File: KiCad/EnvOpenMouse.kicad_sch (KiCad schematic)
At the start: 49 parts, among them J1 SKRKAEE020, J2 SKRKAEE020, J3 Conn_01x03_Male, SW1 MouseSwitch, SW2 MouseSwitch, U1 TCR2EF19, U2 LM3671MF 3.3, U3 PMW3360DM-T2QU, U4 RP2040, Y1 Crystal 3225 12MHz

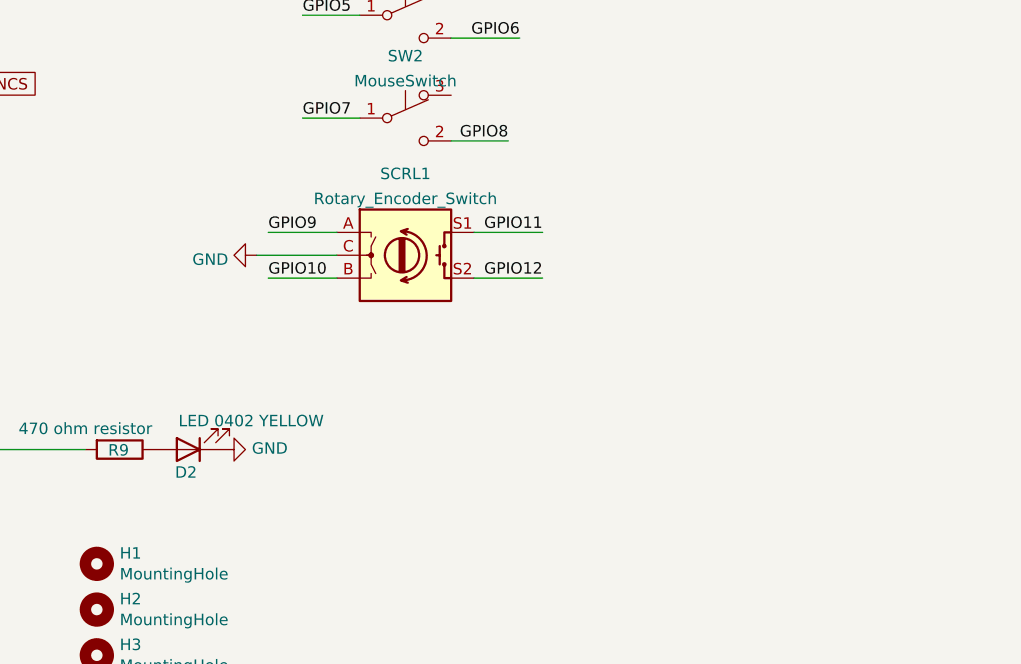
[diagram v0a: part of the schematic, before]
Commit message: added some GPIO headers
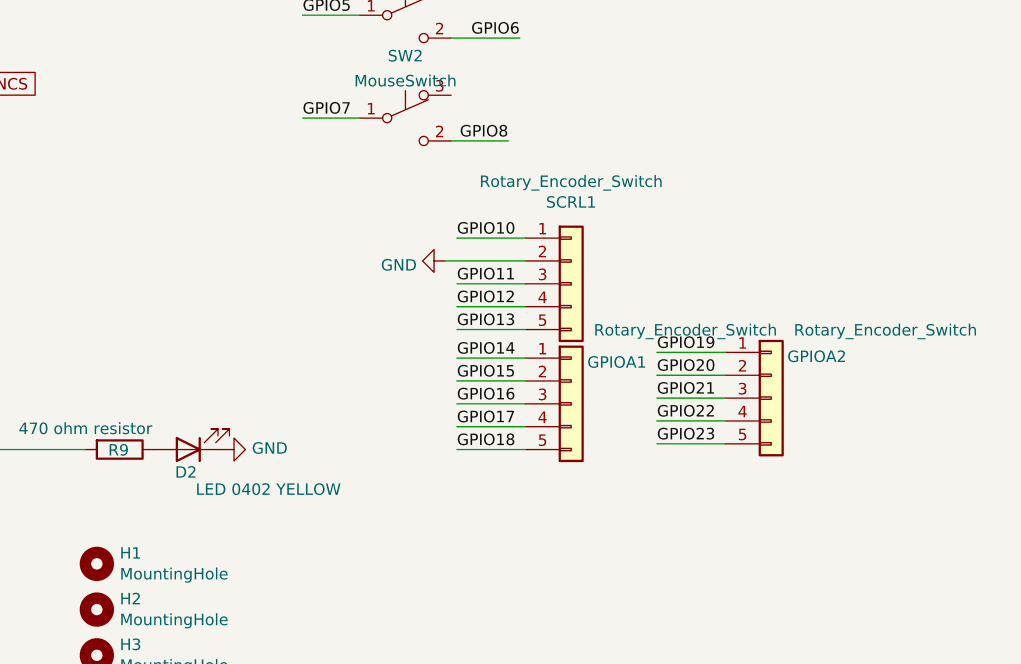
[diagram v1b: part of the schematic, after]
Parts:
- added GPIOA1, GPIOA2: Rotary_Encoder_Switch, Connector_PinHeader_2.54mm:PinHeader_1x05_P2.54mm_Vertical, symbol Connector_Generic:Conn_01x05
- SCRL1: footprint (none) -> Connector_PinHeader_2.54mm:PinHeader_1x05_P2.54mm_Vertical; symbol Device:Rotary_Encoder_Switch -> Connector_Generic:Conn_01x05
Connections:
- net GND: now also SCRL1.2 (Pin_2); no longer SCRL1.C
- net GPIO10: now also SCRL1.1 (Pin_1); no longer SCRL1.B
- net GPIO11: now also SCRL1.3 (Pin_3); no longer SCRL1.S1
- net GPIO12: now also SCRL1.4 (Pin_4); no longer SCRL1.S2
- net GPIO13: now also SCRL1.5 (Pin_5)
- net GPIO14: now also GPIOA1.1 (Pin_1)
- net GPIO15: now also GPIOA1.2 (Pin_2)
- net GPIO16: now also GPIOA1.3 (Pin_3)
- net GPIO17: now also GPIOA1.4 (Pin_4)
- net GPIO18: now also GPIOA1.5 (Pin_5)
- net GPIO19: now also GPIOA2.1 (Pin_1)
- net GPIO20: now also GPIOA2.2 (Pin_2)
- net GPIO21: now also GPIOA2.3 (Pin_3)
- net GPIO22: now also GPIOA2.4 (Pin_4)
- net GPIO23: now also GPIOA2.5 (Pin_5)
- net NCS: no longer SCRL1.A

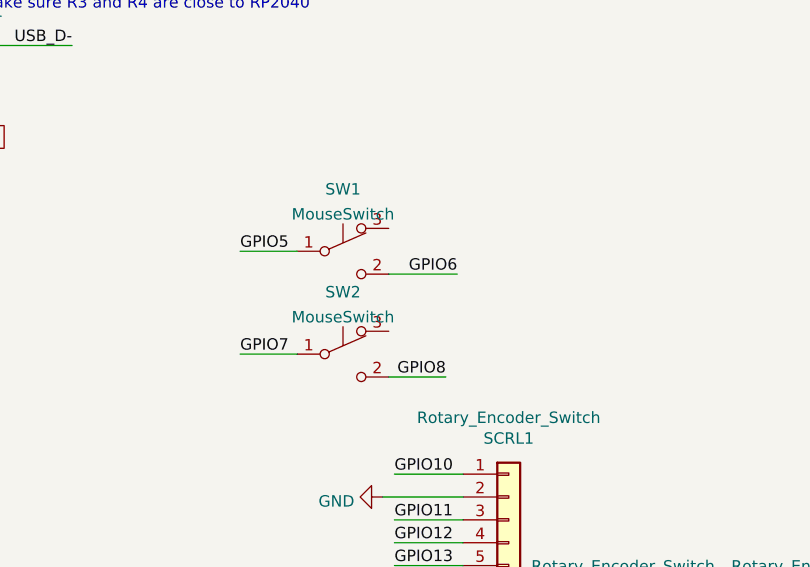
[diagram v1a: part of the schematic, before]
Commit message: swapped button bits for some GPIO headers
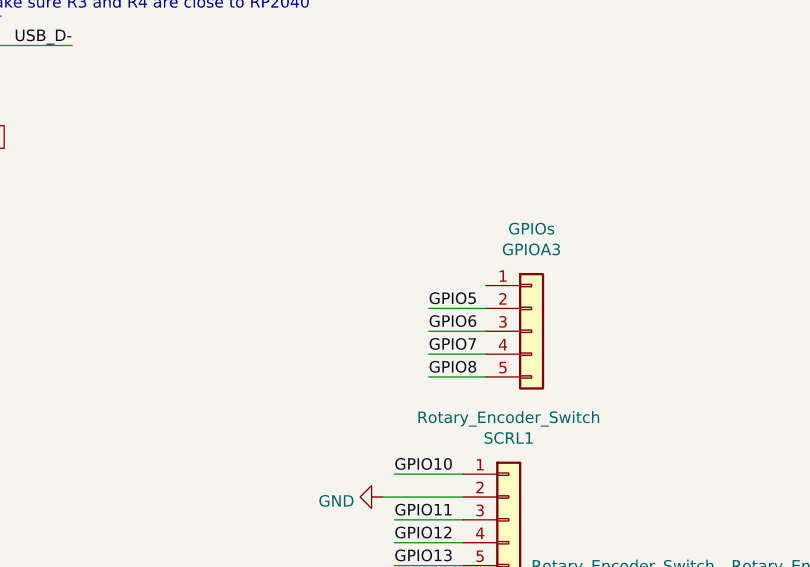
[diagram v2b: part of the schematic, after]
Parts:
- removed SW1, SW2: MouseSwitch, MouseSwitch:MouseSwitch, symbol Switch:SW_Push_SPDT
- added GPIOA3: GPIOs, Connector_PinHeader_2.54mm:PinHeader_1x05_P2.54mm_Vertical, symbol Connector_Generic:Conn_01x05
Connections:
- net GPIO5: now also GPIOA3.2 (Pin_2)
- net GPIO6: now also GPIOA3.3 (Pin_3)
- net GPIO7: now also GPIOA3.4 (Pin_4)
- net GPIO8: now also GPIOA3.5 (Pin_5)
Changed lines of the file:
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@@
-    (stroke (width 0) (type default) (color 0 0 0 0))
-  )
-  (wire (pts (xy 257.81 180.34) (xy 264.16 180.34))
-    (stroke (width 0) (type default) (color 0 0 0 0))
-  )
-  (wire (pts (xy 257.81 191.77) (xy 264.16 191.77))
     (stroke (width 0) (type default) (color 0 0 0 0))
   )
@@
     (stroke (width 0) (type default) (color 0 0 0 0))
   )
-  (wire (pts (xy 274.32 182.88) (xy 281.94 182.88))
-    (stroke (width 0) (type default) (color 0 0 0 0))
-  )
-  (wire (pts (xy 274.32 194.31) (xy 280.67 194.31))
-    (stroke (width 0) (type default) (color 0 0 0 0))
-  )
   (wire (pts (xy 274.701 114.3) (xy 274.701 115.57))
     (stroke (width 0) (type solid) (color 0 0 0 0))
@@
     (stroke (width 0) (type default) (color 0 0 0 0))
   )
+  (wire (pts (xy 278.765 186.69) (xy 285.115 186.69))
+    (stroke (width 0) (type default) (color 0 0 0 0))
+  )
+  (wire (pts (xy 278.765 191.77) (xy 285.115 191.77))
+    (stroke (width 0) (type default) (color 0 0 0 0))
+  )
+  (wire (pts (xy 278.765 194.31) (xy 285.115 194.31))
+    (stroke (width 0) (type default) (color 0 0 0 0))
+  )
   (wire (pts (xy 282.575 210.185) (xy 274.955 210.185))
     (stroke (width 0) (type default) (color 0 0 0 0))
   )
   (wire (pts (xy 282.575 212.725) (xy 274.955 212.725))
+    (stroke (width 0) (type default) (color 0 0 0 0))
+  )
+  (wire (pts (xy 285.115 189.23) (xy 278.765 189.23))
     (stroke (width 0) (type default) (color 0 0 0 0))
   )
@@
     (effects (font (size 1.27 1.27)) (justify right bottom))
   )
-  (label "GPIO5" (at 257.81 180.34 0)
-    (effects (font (size 1.27 1.27)) (justify left bottom))
-  )
-  (label "GPIO7" (at 257.81 191.77 0)
-    (effects (font (size 1.27 1.27)) (justify left bottom))
-  )
   (label "GPIO10" (at 274.955 205.105 0)
     (effects (font (size 1.27 1.27)) (justify left bottom))
@@
     (effects (font (size 1.27 1.27)) (justify left bottom))
   )
-  (label "GPIO8" (at 280.67 194.31 180)
-    (effects (font (size 1.27 1.27)) (justify right bottom))
-  )
-  (label "GPIO6" (at 281.94 182.88 180)
-    (effects (font (size 1.27 1.27)) (justify right bottom))
+  (label "GPIO5" (at 278.765 186.69 0)
+    (effects (font (size 1.27 1.27)) (justify left bottom))
+  )
+  (label "GPIO6" (at 278.765 189.23 0)
+    (effects (font (size 1.27 1.27)) (justify left bottom))
+  )
+  (label "GPIO7" (at 278.765 191.77 0)
+    (effects (font (size 1.27 1.27)) (justify left bottom))
+  )
+  (label "GPIO8" (at 278.765 194.31 0)
+    (effects (font (size 1.27 1.27)) (justify left bottom))
   )
   (label "GPIO19" (at 297.18 217.805 0)
@@
     (pin "3")
   )
-  (symbol (lib_name "SW_Push_SPDT_1") (lib_id "Switch:SW_Push_SPDT") (at 269.24 180.34 0) (unit 1)
-    (in_bom yes) (on_board yes) (fields_autoplaced)
-    (property "Reference" "SW1" (id 0) (at 269.24 173.4525 0))
-    (property "Value" "MouseSwitch" (id 1) (at 269.24 176.2276 0))
-    (property "Footprint" "MouseSwitch:MouseSwitch" (id 2) (at 269.24 180.34 0)
-      (effects (font (size 1.27 1.27)) hide)
-    )
-    (property "Datasheet" "~" (id 3) (at 269.24 180.34 0)
-      (effects (font (size 1.27 1.27)) hide)
-    )
-    (pin "1")
-    (pin "2")
-    (pin "3")
-  )
-  (symbol (lib_name "SW_Push_SPDT_1") (lib_id "Switch:SW_Push_SPDT") (at 269.24 191.77 0) (unit 1)
-    (in_bom yes) (on_board yes) (fields_autoplaced)
-    (property "Reference" "SW2" (id 0) (at 269.24 184.8825 0))
-    (property "Value" "MouseSwitch" (id 1) (at 269.24 187.6576 0))
-    (property "Footprint" "MouseSwitch:MouseSwitch" (id 2) (at 269.24 191.77 0)
-      (effects (font (size 1.27 1.27)) hide)
-    )
-    (property "Datasheet" "~" (id 3) (at 269.24 191.77 0)
-      (effects (font (size 1.27 1.27)) hide)
-    )
-    (pin "1")
-    (pin "2")
-    (pin "3")
-  )
   (symbol (lib_id "logo:LOGO") (at 307.34 264.16 0) (unit 1)
     (in_bom yes) (on_board yes)
@@
     )
     (property "Datasheet" "~" (id 3) (at 287.655 223.52 0)
+      (effects (font (size 1.27 1.27)) hide)
+    )
+    (pin "1")
+    (pin "2")
+    (pin "3")
+    (pin "4")
+    (pin "5")
+  )
+  (symbol (lib_id "Connector_Generic:Conn_01x05") (at 290.195 189.23 0) (unit 1)
+    (in_bom yes) (on_board yes)
+    (property "Reference" "GPIOA3" (id 0) (at 290.195 180.1835 0))
+    (property "Value" "GPIOs" (id 1) (at 290.195 177.8786 0))
+    (property "Footprint" "Connector_PinHeader_2.54mm:PinHeader_1x05_P2.54mm_Vertical" (id 2) (at 290.195 189.23 0)
+      (effects (font (size 1.27 1.27)) hide)
+    )
+    (property "Datasheet" "~" (id 3) (at 290.195 189.23 0)
       (effects (font (size 1.27 1.27)) hide)
     )
@@
       (reference "GPIOA2") (unit 1) (value "Rotary_Encoder_Switch") (footprint "Connector_PinHeader_2.54mm:PinHeader_1x05_P2.54mm_Vertical")
     )
+    (path "/2f2d64a6-47ea-4791-ab5a-ecbf732b2941"
+      (reference "GPIOA3") (unit 1) (value "GPIOs") (footprint "Connector_PinHeader_2.54mm:PinHeader_1x05_P2.54mm_Vertical")
+    )
     (path "/00000000-0000-0000-0000-00005ef4c292"
       (reference "H1") (unit 1) (value "MountingHole") (footprint "MountingHole:MountingHole_2.2mm_M2")
@@
       (reference "SCRL1") (unit 1) (value "Rotary_Encoder_Switch") (footprint "Connector_PinHeader_2.54mm:PinHeader_1x05_P2.54mm_Vertical")
     )
-    (path "/798c83d4-bf59-4ae7-be16-94ab000014d2"
-      (reference "SW1") (unit 1) (value "MouseSwitch") (footprint "MouseSwitch:MouseSwitch")
-    )
-    (path "/9c1369db-a523-40cf-ba52-a05103bcd1ac"
-      (reference "SW2") (unit 1) (value "MouseSwitch") (footprint "MouseSwitch:MouseSwitch")
-    )
     (path "/d68793be-7291-4680-8a60-4689160c349c"

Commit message: decided to overhaul this project a bit
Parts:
- removed C1: 10uf 0603 6.3V, Capacitor_SMD:C_0603_1608Metric, symbol Device:C
- removed C10, C11, C12, C13, C14, C17, C6, C7, C8, C9: 100nf 0402, Capacitor_SMD:C_0402_1005Metric, symbol Device:C
- removed C15, C16: 1uf 0402, Capacitor_SMD:C_0402_1005Metric, symbol Device:C
- removed C18, C19: 22pf 0402, Capacitor_SMD:C_0402_1005Metric, symbol Device:C
- removed C4: 10uf 0402, Capacitor_SMD:C_0402_1005Metric, symbol Device:C
- removed D1: 1n4002 0603, Diode_SMD:D_0603_1608Metric, symbol Device:D_Schottky
- removed D2: LED 0402 YELLOW, LED_SMD:LED_0402_1005Metric, symbol Device:LED
- removed FLASH1: W25Q16FWUXIE, Package_SON:SON-8-1EP_3x2mm_P0.5mm_EP1.4x1.6mm, symbol W25Q256JVEIQ_TR:W25Q256JVEIQ_TR
- removed GPIOA1, GPIOA2, SCRL1: Rotary_Encoder_Switch, Connector_PinHeader_2.54mm:PinHeader_1x05_P2.54mm_Vertical, symbol Connector_Generic:Conn_01x05
- removed GPIOA3: GPIOs, Connector_PinHeader_2.54mm:PinHeader_1x05_P2.54mm_Vertical, symbol Connector_Generic:Conn_01x05
- removed H1, H2, H3, H4: MountingHole, MountingHole:MountingHole_2.2mm_M2, symbol Mechanical:MountingHole
- removed J1, J2: SKRKAEE020, Button_Switch_SMD:SW_Push_SPST_NO_Alps_SKRK, symbol Switch:SW_Push
- removed L1: INDUCTOR 2.2uH 0805, Inductor_SMD:L_0805_2012Metric, symbol pspice:INDUCTOR
- removed R10: 1K 0402, Resistor_SMD:R_0402_1005Metric, symbol Device:R_Small
- removed R2, R4: 5.1K, Resistor_SMD:R_0402_1005Metric, symbol Device:R_Small
- removed R5: 10K 0402, Capacitor_SMD:C_0402_1005Metric, symbol Device:R
- removed R6, R7: 27Ohms 0402 Resistor, Capacitor_SMD:C_0402_1005Metric, symbol Device:R
- removed R8: 1k 0402 Resistor, Capacitor_SMD:C_0402_1005Metric, symbol Device:R
- removed R9: 470 ohm resistor, Resistor_SMD:R_0402_1005Metric, symbol Device:R
- removed U2: LM3671MF 3.3, Package_TO_SOT_SMD:SOT-23-5, symbol Regulator_Switching:LM3670MF
- removed U4: RP2040, env:RP2040-QFN-56, symbol MCU_RaspberryPi_RP2040:RP2040
- removed Y1: Crystal 3225 12MHz, Crystal:Crystal_SMD_3225-4Pin_3.2x2.5mm, symbol Device:Crystal_GND24
- removed e1: TYPE-C-31-M-12, Type-C:HRO-TYPE-C-31-M-12-Assembly, symbol Type-C:HRO-TYPE-C-31-M-12
- added H1, H10, H2, H3, H4, H5, H6, H7, H8, H9: MountingHole_Pad, MountingHole:MountingHole_2.2mm_M2, symbol Mechanical:MountingHole_Pad
- added J1: Conn_01x08, Connector_PinHeader_1.00mm:PinHeader_1x08_P1.00mm_Vertical, symbol Connector_Generic:Conn_01x08
- added J2: Conn_01x03, Connector_PinSocket_2.54mm:PinSocket_1x03_P2.54mm_Vertical, symbol Connector_Generic:Conn_01x03
- added J4: Conn_01x03, Connector_PinHeader_2.54mm:PinHeader_1x03_P2.54mm_Vertical, symbol Connector_Generic:Conn_01x03
- added SW1, SW2: SW_Push_SPDT, MouseSwitch:MouseSwitch, symbol Switch:SW_Push_SPDT
- added VR1: EC10E1220501, EC10E1220501:TRIM_EC10E1220501, symbol EC10E1220501:EC10E1220501
- C1: renamed from C2; footprint Capacitor_SMD:C_0402_1005Metric -> Capacitor_SMD:C_0201_0603Metric
- C2: renamed from C3; footprint Capacitor_SMD:C_0402_1005Metric -> Capacitor_SMD:C_0201_0603Metric
- C3: renamed from C5; footprint Capacitor_SMD:C_0402_1005Metric -> Capacitor_SMD:C_0201_0603Metric
- J3: value Conn_01x03_Male -> Conn_01x03; footprint Connector_PinHeader_2.54mm:PinHeader_1x03_P2.54mm_Vertical -> Connector_PinSocket_2.54mm:PinSocket_1x03_P2.54mm_Vertical
- renumbered R3 to R2, U3 to U2
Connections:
- net +3V3: now also J1.6 (Pin_6)
- net +5V: now also J1.7 (Pin_7)
- net GND: now also H1.1, H10.1, H2.1, H3.1, H4.1, H5.1, H6.1, H7.1, H8.1, H9.1, J1.8 (Pin_8); no longer J3.2 (Pin_2)
- net MISO renamed MISO/GPIO4
- net MISO/GPIO4: now also J1.2 (Pin_2)
- net MOSI renamed MOSI/GPIO3
- net MOSI/GPIO3: now also J1.3 (Pin_3)
- net MOTION renamed MOTION/GPIO1
- net MOTION/GPIO1: now also J1.5 (Pin_5)
- net NCS renamed NCS/GPIO9
- net NCS/GPIO9: now also J1.1 (Pin_1)
- net SCLK renamed SCLK/GPIO2
- net SCLK/GPIO2: now also J1.4 (Pin_4)
- net SWCLK: no longer names the net of J3.1 (Pin_1)
- net SWCLK: now also SW2.1 (A)
- net SWD: no longer names the net of J3.3 (Pin_3)
- net SWD: now also SW2.3 (C)
- new net: J2.1 (Pin_1), SW1.1 (A)
- new net: J2.2 (Pin_2), SW1.2 (B)
- new net: J2.3 (Pin_3), SW1.3 (C)
- new net: J4.1 (Pin_1), VR1.C
- new net: J4.2 (Pin_2), VR1.B
- new net: J4.3 (Pin_3), VR1.A
- new net: J3.2 (Pin_2), SW2.2 (B)
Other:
- note added: "1.8V regulator"
- note added: "Mount Holes"
- note added: "Mouse Buttons"
- note added: "Scroll Wheel"
- note added: "Sensor Header"
- note removed: "2x 5.1K Resistors on the CC pins will = 5V@1.5A this is the recomended default config for type-c"
- note removed: "Crystal"
- note removed: "D1 NEEDS to be 0omh resistor or 1n4002"
- note removed: "Flash"
- note removed: "Im pretty sure a lot of these W25QXXX Chips are pin compatible Dont quote me on that"
- note removed: "Im unsure if the RP2040 can function with flash larger than 128Mb"
- note removed: "KoreanHROParts USB_C_Receptacle_HRO_TYPE-C-31-M-12"
- note removed: "Make sure C10 is close to pin 44 of RP2040"
- note removed: "Make sure C3 is close to pin 45 of RP2040"
- note removed: "Make sure R3 and R4 are close to RP2040"
- note removed: "Pin 9 technically doesnt exist its the main central contact under the chip for heat dicipation"
- note removed: "These decoupling capacitors are meant to be put close by each 3.3V pin of the RP2040"
- note removed: "USB/POWER"
- note removed: "the max frequency is 15mhz so something about 8 to 12Mhz seems good."
- note removed: "this is for factory testing always pull this to ground"
- moved on the sheet: C1, C2, C3, R1, R2, U1, U2

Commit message: small fix
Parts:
- J2, J3: footprint Connector_PinSocket_2.54mm:PinSocket_1x03_P2.54mm_Vertical -> Connector_PinHeader_2.54mm:PinHeader_1x03_P2.54mm_Vertical
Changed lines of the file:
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@@
       (effects (font (size 1.27 1.27)) (justify left))
     )
-    (property "Footprint" "Connector_PinSocket_2.54mm:PinSocket_1x03_P2.54mm_Vertical" (id 2) (at 37.465 70.485 0)
+    (property "Footprint" "Connector_PinHeader_2.54mm:PinHeader_1x03_P2.54mm_Vertical" (id 2) (at 37.465 70.485 0)
       (effects (font (size 1.27 1.27)) hide)
     )
@@
       (effects (font (size 1.27 1.27)) (justify left))
     )
-    (property "Footprint" "Connector_PinSocket_2.54mm:PinSocket_1x03_P2.54mm_Vertical" (id 2) (at 37.465 87.63 0)
+    (property "Footprint" "Connector_PinHeader_2.54mm:PinHeader_1x03_P2.54mm_Vertical" (id 2) (at 37.465 87.63 0)
       (effects (font (size 1.27 1.27)) hide)
     )
@@
     )
     (path "/98f1a8e5-ac0b-4fdf-8673-39af51bc1be8"
-      (reference "J2") (unit 1) (value "Conn_01x03") (footprint "Connector_PinSocket_2.54mm:PinSocket_1x03_P2.54mm_Vertical")
+      (reference "J2") (unit 1) (value "Conn_01x03") (footprint "Connector_PinHeader_2.54mm:PinHeader_1x03_P2.54mm_Vertical")
     )
     (path "/7e8df33d-f37a-411b-9ba7-24c22f5de4d0"
-      (reference "J3") (unit 1) (value "Conn_01x03") (footprint "Connector_PinSocket_2.54mm:PinSocket_1x03_P2.54mm_Vertical")
+      (reference "J3") (unit 1) (value "Conn_01x03") (footprint "Connector_PinHeader_2.54mm:PinHeader_1x03_P2.54mm_Vertical")
     )
     (path "/76279e70-cee9-478d-a7fa-28cc1e1399ab"

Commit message: added missing capactor and middle click button.
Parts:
- added C4: 100nf 0402, Capacitor_SMD:C_0201_0603Metric, symbol Device:C_Small
- added J5: Conn_01x03, Connector_PinHeader_2.54mm:PinHeader_1x03_P2.54mm_Vertical, symbol Connector_Generic:Conn_01x03
- added SW3: SW_Push_SPDT, MouseSwitch:MouseSwitch, symbol Switch:SW_Push_SPDT
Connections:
- net GND: now also C4.2
- net at C3.1, U2.3 (VDDPIX): now also C4.1
- new net: J5.1 (Pin_1), SW3.1 (A)
- new net: J5.2 (Pin_2), SW3.2 (B)
- new net: J5.3 (Pin_3), SW3.3 (C)

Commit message: Appended RP2040 to board, begin work on Mouse PCB
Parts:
- removed H1, H2, H3, H4, H5, H6: MountingHole_Pad, MountingHole:MountingHole_2.2mm_M2, symbol Mechanical:MountingHole_Pad
- U1: value TCR2EF19 -> TLV70218DBVR
- renumbered C4 to C3, C3 to C4, H7 to H1, H8 to H2, H9 to H3, H10 to H4
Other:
- added sheet RP2040 (RP2040MCU.kicad_sch)

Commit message: routed onboard MCU
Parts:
- removed J1: Conn_01x08, Connector_PinHeader_1.00mm:PinHeader_1x08_P1.00mm_Vertical, symbol Connector_Generic:Conn_01x08
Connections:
- net +5V renamed VBUS
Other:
- note removed: "Sensor Header"

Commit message: I dont even remember what I changed.
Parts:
- removed J2, J3, J4, J5: Conn_01x03, Connector_PinHeader_2.54mm:PinHeader_1x03_P2.54mm_Vertical, symbol Connector_Generic:Conn_01x03
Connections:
- net GND: now also VR1.B
- net MB-1-A: now reaches SW1.1 (A)
- net MB-1-B: now reaches SW1.2 (B)
- net ROT-B: now reaches VR1.C
- net ROT-A: now reaches VR1.A
- net MB-2-A: now reaches SW2.1 (A)
- net MB-2-B: now reaches SW2.2 (B)
- net MB-3-A: now reaches SW3.1 (A)
- net MB-3-B: now reaches SW3.2 (B)
